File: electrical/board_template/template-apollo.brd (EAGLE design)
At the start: 1 part

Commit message: new version of template board
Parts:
- added U$1: BOARD_TEMPLATE1, template_board:BOARD_TEMPLATE
- moved JP1 0.15 mm to (45.0, 45.0)
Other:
- board outline added: 88 x 88 mm
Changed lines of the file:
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@@
 <setting verticaltext="up"/>
 </settings>
-<grid distance="1" unitdist="mm" unit="mm" style="lines" multiple="1" display="yes" altdistance="5" altunitdist="mil" altunit="mil"/>
+<grid distance="1" unitdist="mm" unit="mm" style="lines" multiple="1" display="yes" altdistance="0.1" altunitdist="mm" altunit="mm"/>
 <layers>
 <layer number="1" name="Top" color="4" fill="1" visible="yes" active="yes"/>
@@
 <board>
 <plain>
-<dimension x1="0.8042" y1="3.9032" x2="89.0656" y2="3.9088" x3="44.935465625" y3="-5.002796875" textsize="1.778" layer="1"/>
-<dimension x1="3.90958125" y1="0.79781875" x2="4" y2="89" x3="-11.04416875" y3="44.91428125" textsize="1.778" layer="1"/>
 </plain>
 <attributes>
@@
 </autorouter>
 <elements>
-<element name="JP1" library="DubSat1 Components latest" package="PC104_CONNECTOR" value="PC104_CONNECTOR" x="44.9552" y="45.1424" smashed="yes"/>
+<element name="JP1" library="DubSat1 Components latest" package="PC104_CONNECTOR" value="PC104_CONNECTOR" x="44.9952" y="45.0024" smashed="yes"/>
+<element name="U$1" library="template_board" package="BOARD_TEMPLATE" value="BOARD_TEMPLATE1" x="45" y="45" smashed="yes"/>
 </elements>
 <signals>
 <signal name="GND">
 <polygon width="0.254" layer="16" isolate="0.2032">
-<vertex x="3.9248" y="89.0496"/>
-<vertex x="85.9856" y="89.0496"/>
-<vertex x="89.0656" y="85.9696"/>
-<vertex x="89.0656" y="3.9088"/>
-<vertex x="85.98598125" y="0.82918125"/>
-<vertex x="3.90958125" y="0.79781875"/>
-<vertex x="0.8042" y="3.9032"/>
-<vertex x="0.8042" y="85.929"/>
+<vertex x="4.06" y="88.87"/>
+<vertex x="85.9452" y="88.87"/>
+<vertex x="88.8656" y="85.9496"/>
+<vertex x="88.8656" y="4.0488"/>
+<vertex x="85.9758875" y="1.1590875"/>
+<vertex x="4.0592125" y="1.1277875"/>
+<vertex x="1.139" y="4.048"/>
+<vertex x="1.139" y="85.949"/>
 </polygon>
 <contactref element="JP1" pad="P$94"/>
 <polygon width="0.254" layer="1" isolate="0.3048" rank="6">
-<vertex x="4.1026" y="1.4892"/>
-<vertex x="1.302" y="4.2898"/>
-<vertex x="1.302" y="85.995"/>
-<vertex x="4.1026" y="88.7956"/>
-<vertex x="85.8078" y="88.7956"/>
-<vertex x="88.6084" y="85.995"/>
-<vertex x="88.6084" y="4.2898"/>
-<vertex x="85.8078" y="1.4892"/>
+<vertex x="4.0578" y="1.1292"/>
+<vertex x="1.1396" y="4.0474"/>
+<vertex x="1.1396" y="85.9526"/>
+<vertex x="4.0526" y="88.8656"/>
+<vertex x="85.9478" y="88.8656"/>
+<vertex x="88.8684" y="85.945"/>
+<vertex x="88.8684" y="4.0498"/>
+<vertex x="85.9478" y="1.1292"/>
 </polygon>
 </signal>
@@
 </board>
 </drawing>
+<compatibility>
+<note version="8.3" severity="warning">
+Since Version 8.3, EAGLE supports URNs for individual library
+assets (packages, symbols, and devices). The URNs of those assets
+will not be understood (or retained) with this version.
+</note>
+</compatibility>
 </eagle>

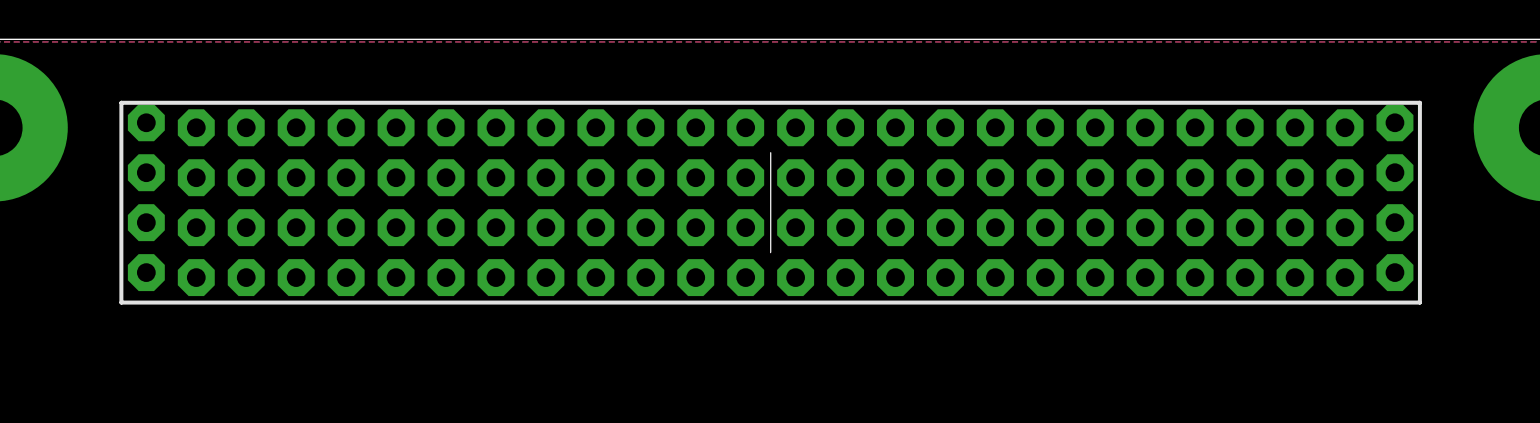
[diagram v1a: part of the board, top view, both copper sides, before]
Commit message: fix template board symbols
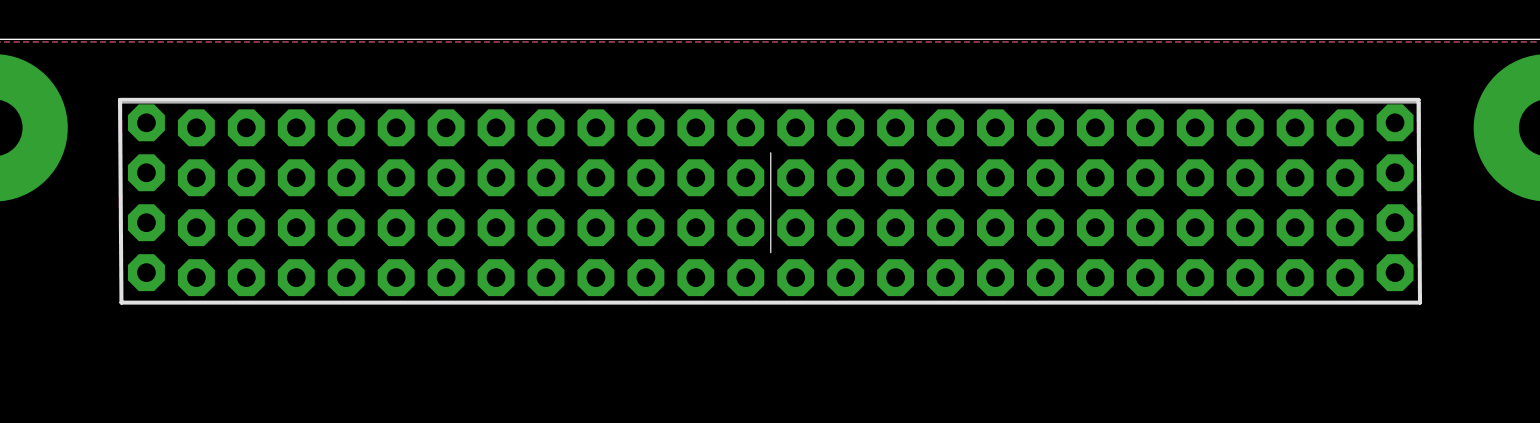
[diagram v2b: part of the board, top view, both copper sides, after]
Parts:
- removed JP1: PC104_CONNECTOR, DubSat1 Components latest:PC104_CONNECTOR
- added U$2: PC104_CONNECTOR, template_board:PC104_CONNECTOR
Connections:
- removed net CANH: JP1.P$53
- removed net CANL: JP1.P$57
- removed net GND: JP1.P$94
- removed net VBAT: JP1.P$93
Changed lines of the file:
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@@
 </autorouter>
 <elements>
-<element name="JP1" library="DubSat1 Components latest" package="PC104_CONNECTOR" value="PC104_CONNECTOR" x="44.9952" y="45.0024" smashed="yes"/>
 <element name="U$1" library="template_board" package="BOARD_TEMPLATE" value="BOARD_TEMPLATE1" x="45" y="45" smashed="yes"/>
+<element name="U$2" library="template_board" package="PC104_CONNECTOR" value="PC104_CONNECTOR" x="45" y="45" smashed="yes"/>
 </elements>
 <signals>
@@
 <vertex x="1.139" y="85.949"/>
 </polygon>
-<contactref element="JP1" pad="P$94"/>
 <polygon width="0.254" layer="1" isolate="0.3048" rank="6">
 <vertex x="4.0578" y="1.1292"/>
@@
 </polygon>
 </signal>
-<signal name="CANL">
-<contactref element="JP1" pad="P$57"/>
-</signal>
-<signal name="CANH">
-<contactref element="JP1" pad="P$53"/>
-</signal>
-<signal name="VBAT">
-<contactref element="JP1" pad="P$93"/>
-</signal>
 </signals>
